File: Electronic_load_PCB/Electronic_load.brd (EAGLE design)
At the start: 121.9 x 88.6 mm, 111 parts, among them IC7 LM1117IMPX-5.0, J1 XT60-M, J2 B2B-XH, J3 B4B-XH, J4 B2B-XH, J5 B2B-XH, J6 B2B-XH, J7 B2B-XH, J8 B5B-XH, Q1 IRFP250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

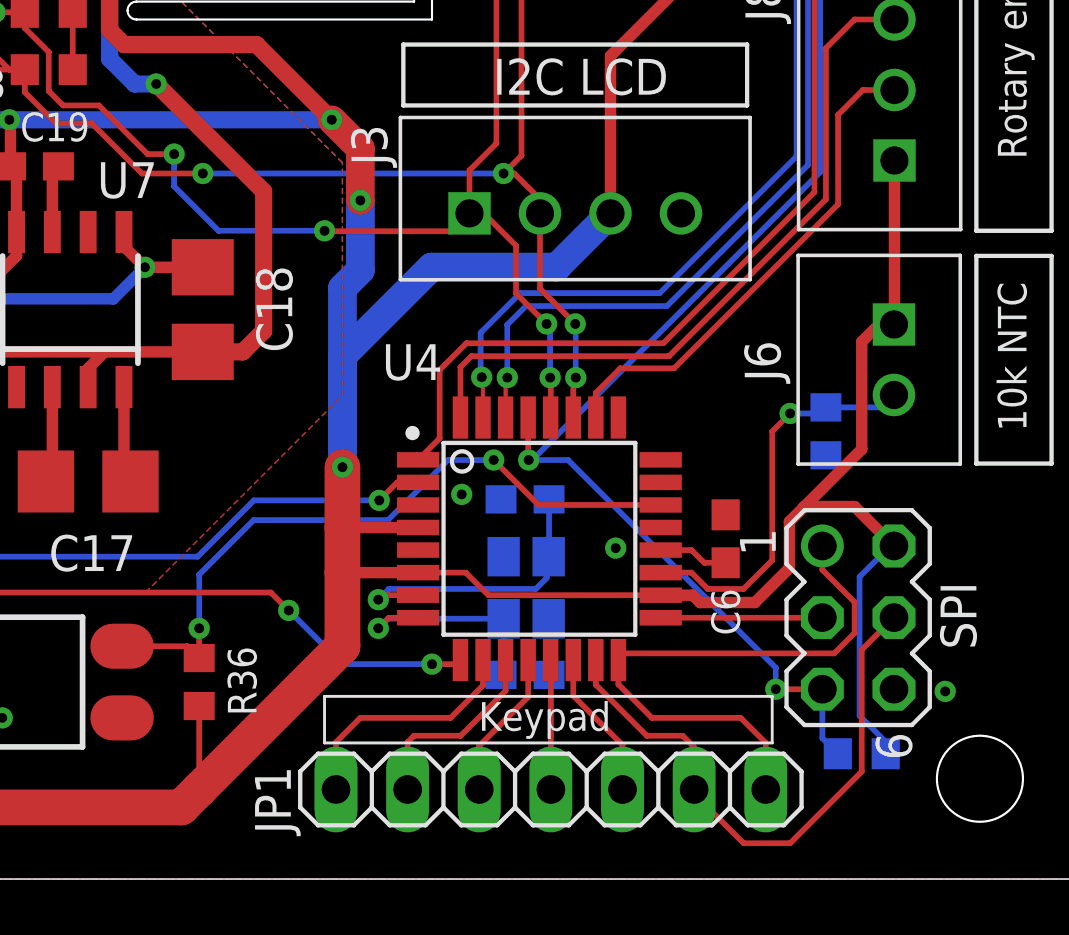
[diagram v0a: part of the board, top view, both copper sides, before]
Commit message: 9 pin keypad
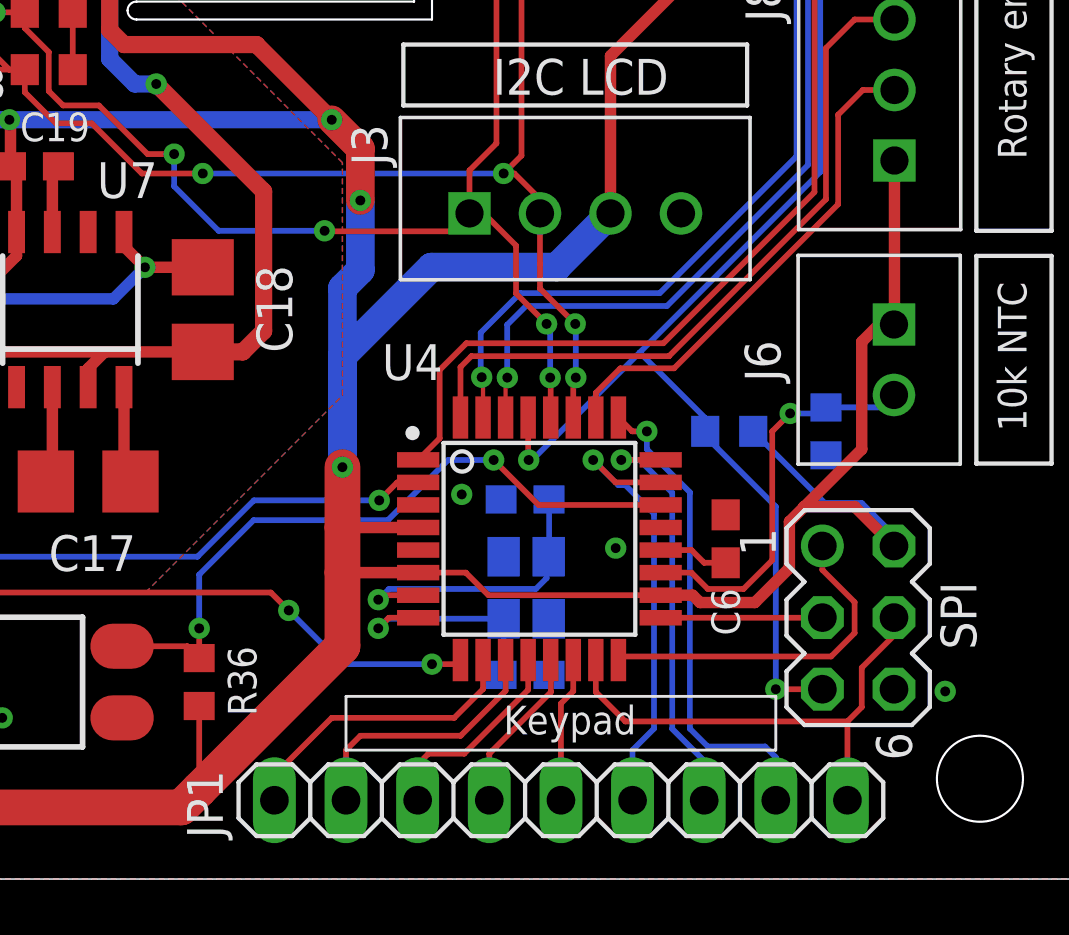
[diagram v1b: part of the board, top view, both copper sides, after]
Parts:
- JP1: device pinhead:1X07 -> pinhead:1X09
- moved R29 12.4 mm to (109.6, 15.9)
- moved JP1 0.52 mm to (103.6, 2.79)
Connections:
- removed net KP6/MOSI: JP1.6, SPI.4, U4.15
- removed net KP7/MISO: JP1.7, SPI.1, U4.16
- new net KP6: JP1.6, U4.23
- new net KP7: JP1.7, U4.24
- new net KP8: JP1.8, U4.25
- new net KP9/MOSI: JP1.9, SPI.4, U4.15
- new net MISO: SPI.1, U4.16
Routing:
- net KP7/MISO: track 20.9 -> 0.00 mm
- net KP6/MOSI: track 20.6 -> 0.00 mm
- net KP9/MOSI: track 0.00 -> 17.6 mm
- net KP8: track 0.00 -> 17.4 mm, vias 0 -> 1
- net KP6: track 0.00 -> 16.1 mm, vias 0 -> 1
- net KP7: track 0.00 -> 15.1 mm, vias 0 -> 1
- net MISO: track 0.00 -> 12.3 mm
- net KP2: track 7.00 -> 9.40 mm
- net KP3: track 5.31 -> 7.34 mm
- net KP1: track 8.62 -> 10.6 mm
- net 5V: track 278.3 -> 276.8 mm
- net KP4: track 4.59 -> 5.88 mm
- net RST: track 51.0 -> 50.0 mm

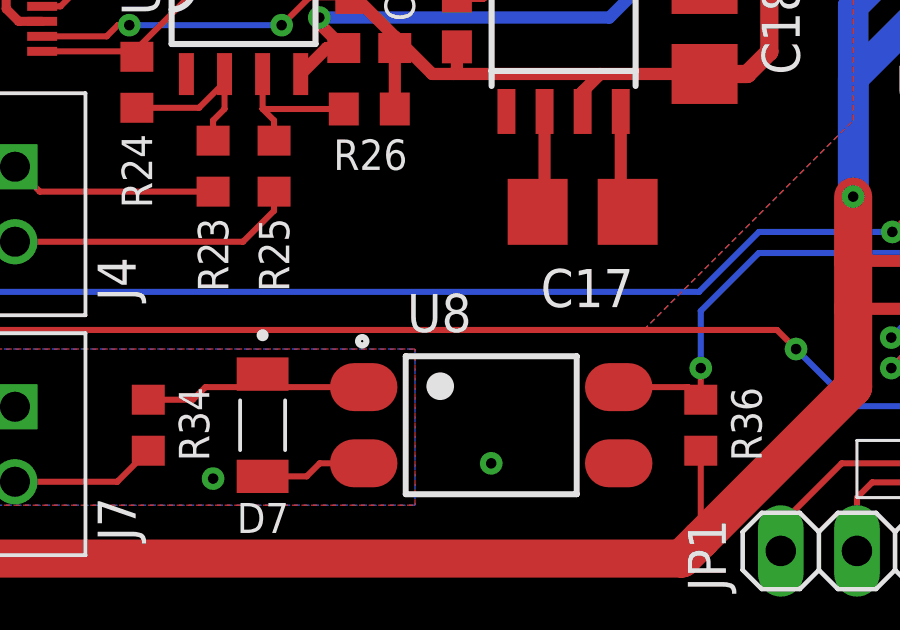
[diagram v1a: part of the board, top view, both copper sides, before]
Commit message: added missing component values
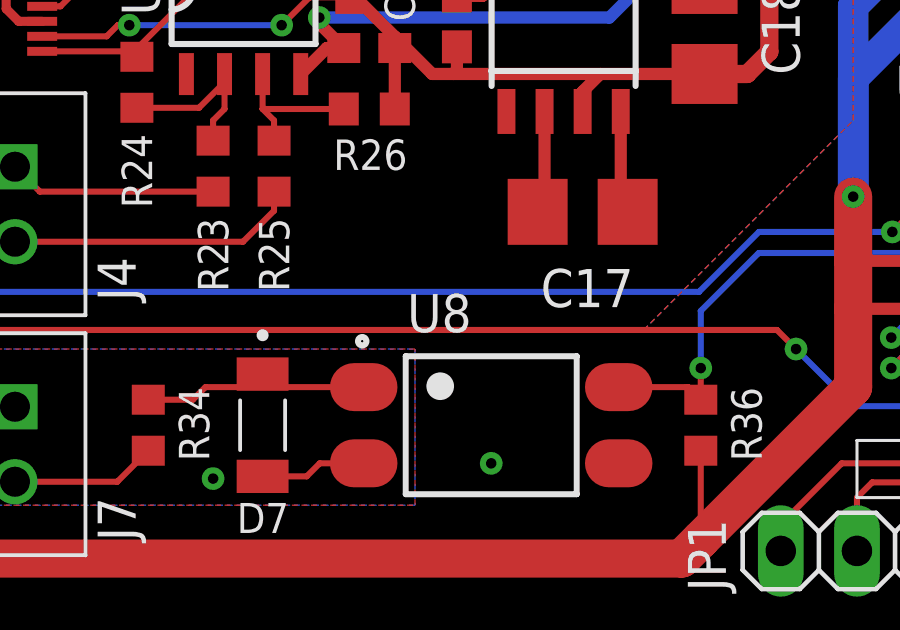
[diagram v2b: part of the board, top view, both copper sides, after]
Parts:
- R21: value (none) -> 15k
- R22, R41, R42, R43, R44: value (none) -> 1k
- R30: value (none) -> 470R
- R32: value 1k -> 68k
- R33: value 1k -> 18k
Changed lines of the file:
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@@
 <attribute name="VALUE" x="78.661" y="32.798" size="1.27" layer="27" rot="R180" align="bottom-right"/>
 </element>
-<element name="R21" library="rcl" library_urn="urn:adsk.eagle:library:334" package="R0603" package3d_urn="urn:adsk.eagle:package:23555/3" value="" x="77.851" y="35.814" smashed="yes">
+<element name="R21" library="rcl" library_urn="urn:adsk.eagle:library:334" package="R0603" package3d_urn="urn:adsk.eagle:package:23555/3" value="15k" x="77.851" y="35.814" smashed="yes">
 <attribute name="NAME" x="76.708" y="36.703" size="1.016" layer="25"/>
 <attribute name="POPULARITY" value="70" x="77.851" y="35.814" size="1.778" layer="27" display="off"/>
@@
 <attribute name="VALUE" x="77.216" y="33.909" size="1.27" layer="27"/>
 </element>
-<element name="R22" library="rcl" library_urn="urn:adsk.eagle:library:334" package="R0603" package3d_urn="urn:adsk.eagle:package:23555/3" value="" x="75.311" y="34.29" smashed="yes" rot="R90">
+<element name="R22" library="rcl" library_urn="urn:adsk.eagle:library:334" package="R0603" package3d_urn="urn:adsk.eagle:package:23555/3" value="1k" x="75.311" y="34.29" smashed="yes" rot="R90">
 <attribute name="NAME" x="75.819" y="30.099" size="1.016" layer="25" rot="R90"/>
 <attribute name="POPULARITY" value="70" x="75.311" y="34.29" size="1.778" layer="27" rot="R90" display="off"/>
@@
 <attribute name="VALUE" x="26.035" y="32.385" size="1.27" layer="28" rot="MR270"/>
 </element>
-<element name="R30" library="rcl" library_urn="urn:adsk.eagle:library:334" package="R0603" package3d_urn="urn:adsk.eagle:package:23555/3" value="" x="34.925" y="29.845" smashed="yes" rot="R90">
+<element name="R30" library="rcl" library_urn="urn:adsk.eagle:library:334" package="R0603" package3d_urn="urn:adsk.eagle:package:23555/3" value="470R" x="34.925" y="29.845" smashed="yes" rot="R90">
 <attribute name="NAME" x="36.83" y="28.575" size="1.016" layer="25" rot="R90"/>
 <attribute name="POPULARITY" value="70" x="34.925" y="29.845" size="1.778" layer="27" rot="R90" display="off"/>
@@
 <attribute name="VALUE" x="29.845" y="17.78" size="1.27" layer="28" rot="MR180"/>
 </element>
-<element name="R32" library="rcl" library_urn="urn:adsk.eagle:library:334" package="R0603" package3d_urn="urn:adsk.eagle:package:23555/3" value="1k" x="25.4" y="17.145" smashed="yes" rot="R90">
+<element name="R32" library="rcl" library_urn="urn:adsk.eagle:library:334" package="R0603" package3d_urn="urn:adsk.eagle:package:23555/3" value="68k" x="25.4" y="17.145" smashed="yes" rot="R90">
 <attribute name="NAME" x="24.13" y="15.875" size="1.016" layer="25" rot="R90"/>
 <attribute name="POPULARITY" value="70" x="25.4" y="17.145" size="1.778" layer="27" rot="R90" display="off"/>
@@
 <attribute name="VALUE" x="27.305" y="16.51" size="1.27" layer="27" rot="R90"/>
 </element>
-<element name="R33" library="rcl" library_urn="urn:adsk.eagle:library:334" package="R0603" package3d_urn="urn:adsk.eagle:package:23555/3" value="1k" x="25.4" y="20.32" smashed="yes" rot="R90">
+<element name="R33" library="rcl" library_urn="urn:adsk.eagle:library:334" package="R0603" package3d_urn="urn:adsk.eagle:package:23555/3" value="18k" x="25.4" y="20.32" smashed="yes" rot="R90">
 <attribute name="NAME" x="24.13" y="19.05" size="1.016" layer="25" rot="R90"/>
 <attribute name="POPULARITY" value="70" x="25.4" y="20.32" size="1.778" layer="27" rot="R90" display="off"/>
@@
 <attribute name="MF" value="Sharp Microelectronics" x="83.82" y="6.985" size="1.778" layer="27" display="off"/>
 <attribute name="MP" value="PC817X2NIP0F" x="83.82" y="6.985" size="1.778" layer="27" display="off"/>
+<attribute name="NAME" x="81.014759375" y="10.0908" size="1.27238125" layer="25"/>
 <attribute name="NAME" x="81.01816875" y="10.08701875" size="1.27083125" layer="25"/>
-<attribute name="NAME" x="81.014759375" y="10.0908" size="1.27238125" layer="25"/>
 <attribute name="PACKAGE" value="SMD-4 Sharp" x="83.82" y="6.985" size="1.778" layer="27" display="off"/>
 <attribute name="PRICE" value="None" x="83.82" y="6.985" size="1.778" layer="27" display="off"/>
@@
 <attribute name="VALUE" x="118.11" y="40.005" size="1.27" layer="27" rot="R90"/>
 </element>
-<element name="R41" library="rcl" library_urn="urn:adsk.eagle:library:334" package="R0603" package3d_urn="urn:adsk.eagle:package:23555/3" value="" x="62.738" y="22.86" smashed="yes" rot="R90">
+<element name="R41" library="rcl" library_urn="urn:adsk.eagle:library:334" package="R0603" package3d_urn="urn:adsk.eagle:package:23555/3" value="1k" x="62.738" y="22.86" smashed="yes" rot="R90">
 <attribute name="NAME" x="63.246" y="24.384" size="1.016" layer="25" rot="R90"/>
 <attribute name="POPULARITY" value="70" x="62.738" y="22.86" size="1.778" layer="27" rot="R90" display="off"/>
@@
 <attribute name="VALUE" x="64.643" y="22.225" size="1.27" layer="27" rot="R90"/>
 </element>
-<element name="R42" library="rcl" library_urn="urn:adsk.eagle:library:334" package="R0603" package3d_urn="urn:adsk.eagle:package:23555/3" value="" x="60.706" y="22.86" smashed="yes" rot="R90">
+<element name="R42" library="rcl" library_urn="urn:adsk.eagle:library:334" package="R0603" package3d_urn="urn:adsk.eagle:package:23555/3" value="1k" x="60.706" y="22.86" smashed="yes" rot="R90">
 <attribute name="NAME" x="61.214" y="24.384" size="1.016" layer="25" rot="R90"/>
 <attribute name="POPULARITY" value="70" x="60.706" y="22.86" size="1.778" layer="27" rot="R90" display="off"/>
@@
 <attribute name="VALUE" x="62.611" y="22.225" size="1.27" layer="27" rot="R90"/>
 </element>
-<element name="R43" library="rcl" library_urn="urn:adsk.eagle:library:334" package="R0603" package3d_urn="urn:adsk.eagle:package:23555/3" value="" x="58.674" y="22.86" smashed="yes" rot="R90">
+<element name="R43" library="rcl" library_urn="urn:adsk.eagle:library:334" package="R0603" package3d_urn="urn:adsk.eagle:package:23555/3" value="1k" x="58.674" y="22.86" smashed="yes" rot="R90">
 <attribute name="NAME" x="59.182" y="24.384" size="1.016" layer="25" rot="R90"/>
 <attribute name="POPULARITY" value="70" x="58.674" y="22.86" size="1.778" layer="27" rot="R90" display="off"/>
@@
 <attribute name="VALUE" x="60.579" y="22.225" size="1.27" layer="27" rot="R90"/>
 </element>
-<element name="R44" library="rcl" library_urn="urn:adsk.eagle:library:334" package="R0603" package3d_urn="urn:adsk.eagle:package:23555/3" value="" x="56.642" y="22.86" smashed="yes" rot="R90">
+<element name="R44" library="rcl" library_urn="urn:adsk.eagle:library:334" package="R0603" package3d_urn="urn:adsk.eagle:package:23555/3" value="1k" x="56.642" y="22.86" smashed="yes" rot="R90">
 <attribute name="NAME" x="57.15" y="24.384" size="1.016" layer="25" rot="R90"/>
 <attribute name="POPULARITY" value="70" x="56.642" y="22.86" size="1.778" layer="27" rot="R90" display="off"/>

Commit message: changed some resistor values
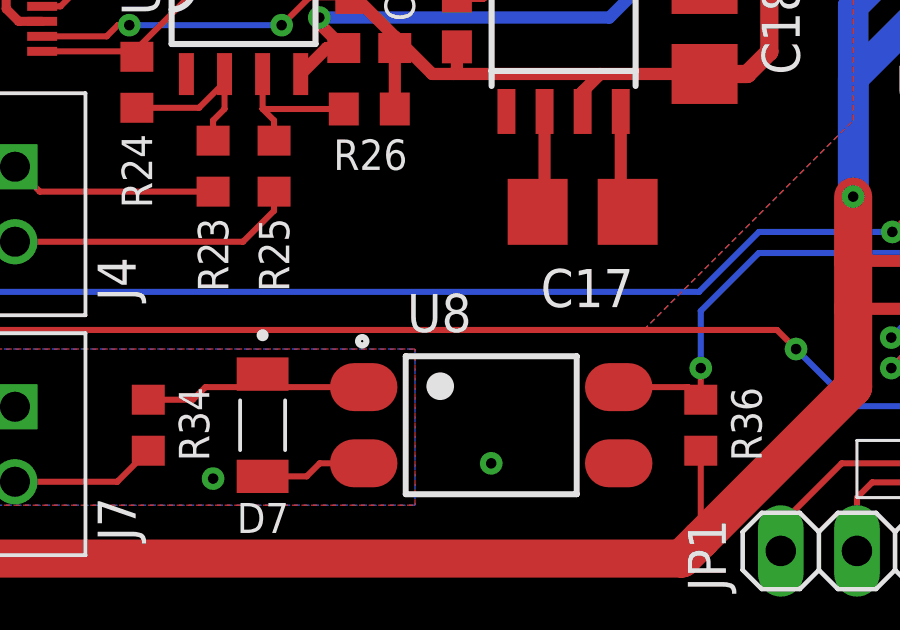
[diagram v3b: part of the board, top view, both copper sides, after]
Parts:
- R21: value 15k -> 10k
- R30: value 470R -> 1k
- R35: value 10k -> 47k
- R37, R38, R39, R40: value 1k -> 100k
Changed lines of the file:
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@@
 <attribute name="VALUE" x="78.661" y="32.798" size="1.27" layer="27" rot="R180" align="bottom-right"/>
 </element>
-<element name="R21" library="rcl" library_urn="urn:adsk.eagle:library:334" package="R0603" package3d_urn="urn:adsk.eagle:package:23555/3" value="15k" x="77.851" y="35.814" smashed="yes">
+<element name="R21" library="rcl" library_urn="urn:adsk.eagle:library:334" package="R0603" package3d_urn="urn:adsk.eagle:package:23555/3" value="10k" x="77.851" y="35.814" smashed="yes">
 <attribute name="NAME" x="76.708" y="36.703" size="1.016" layer="25"/>
 <attribute name="POPULARITY" value="70" x="77.851" y="35.814" size="1.778" layer="27" display="off"/>
@@
 <attribute name="VALUE" x="26.035" y="32.385" size="1.27" layer="28" rot="MR270"/>
 </element>
-<element name="R30" library="rcl" library_urn="urn:adsk.eagle:library:334" package="R0603" package3d_urn="urn:adsk.eagle:package:23555/3" value="470R" x="34.925" y="29.845" smashed="yes" rot="R90">
+<element name="R30" library="rcl" library_urn="urn:adsk.eagle:library:334" package="R0603" package3d_urn="urn:adsk.eagle:package:23555/3" value="1k" x="34.925" y="29.845" smashed="yes" rot="R90">
 <attribute name="NAME" x="36.83" y="28.575" size="1.016" layer="25" rot="R90"/>
 <attribute name="POPULARITY" value="70" x="34.925" y="29.845" size="1.778" layer="27" rot="R90" display="off"/>
@@
 <attribute name="VALUE" x="70.485" y="7.62" size="1.27" layer="27" rot="R270"/>
 </element>
-<element name="R35" library="rcl" library_urn="urn:adsk.eagle:library:334" package="R0603" package3d_urn="urn:adsk.eagle:package:23555/3" value="10k" x="113.03" y="15.875" smashed="yes" rot="MR90">
+<element name="R35" library="rcl" library_urn="urn:adsk.eagle:library:334" package="R0603" package3d_urn="urn:adsk.eagle:package:23555/3" value="47k" x="113.03" y="15.875" smashed="yes" rot="MR90">
 <attribute name="NAME" x="112.4966" y="17.4244" size="1.016" layer="26" rot="MR90"/>
 <attribute name="POPULARITY" value="70" x="113.03" y="15.875" size="1.778" layer="28" rot="MR90" display="off"/>
@@
 <attribute name="MF" value="Sharp Microelectronics" x="83.82" y="6.985" size="1.778" layer="27" display="off"/>
 <attribute name="MP" value="PC817X2NIP0F" x="83.82" y="6.985" size="1.778" layer="27" display="off"/>
+<attribute name="NAME" x="81.01816875" y="10.08701875" size="1.27083125" layer="25"/>
 <attribute name="NAME" x="81.014759375" y="10.0908" size="1.27238125" layer="25"/>
-<attribute name="NAME" x="81.01816875" y="10.08701875" size="1.27083125" layer="25"/>
 <attribute name="PACKAGE" value="SMD-4 Sharp" x="83.82" y="6.985" size="1.778" layer="27" display="off"/>
 <attribute name="PRICE" value="None" x="83.82" y="6.985" size="1.778" layer="27" display="off"/>
@@
 <attribute name="VALUE" x="57.785" y="36.449" size="1.27" layer="28" rot="MR270"/>
 </element>
-<element name="R37" library="rcl" library_urn="urn:adsk.eagle:library:334" package="R0603" package3d_urn="urn:adsk.eagle:package:23555/3" value="1k" x="58.42" y="34.925" smashed="yes" rot="MR0">
+<element name="R37" library="rcl" library_urn="urn:adsk.eagle:library:334" package="R0603" package3d_urn="urn:adsk.eagle:package:23555/3" value="100k" x="58.42" y="34.925" smashed="yes" rot="MR0">
 <attribute name="NAME" x="62.484" y="34.417" size="1.016" layer="26" rot="MR0"/>
 <attribute name="POPULARITY" value="70" x="58.42" y="34.925" size="1.016" layer="28" rot="MR0" display="off"/>
@@
 <attribute name="VALUE" x="57.785" y="32.385" size="1.27" layer="28" rot="MR270"/>
 </element>
-<element name="R38" library="rcl" library_urn="urn:adsk.eagle:library:334" package="R0603" package3d_urn="urn:adsk.eagle:package:23555/3" value="1k" x="58.42" y="36.957" smashed="yes" rot="MR0">
+<element name="R38" library="rcl" library_urn="urn:adsk.eagle:library:334" package="R0603" package3d_urn="urn:adsk.eagle:package:23555/3" value="100k" x="58.42" y="36.957" smashed="yes" rot="MR0">
 <attribute name="NAME" x="62.484" y="36.576" size="1.016" layer="26" rot="MR0"/>
 <attribute name="POPULARITY" value="70" x="66.04" y="44.577" size="1.016" layer="28" rot="MR0" display="off"/>
@@
 <attribute name="VALUE" x="65.405" y="27.051" size="1.27" layer="28" rot="MR90"/>
 </element>
-<element name="R39" library="rcl" library_urn="urn:adsk.eagle:library:334" package="R0603" package3d_urn="urn:adsk.eagle:package:23555/3" value="1k" x="67.818" y="32.004" smashed="yes" rot="MR180">
+<element name="R39" library="rcl" library_urn="urn:adsk.eagle:library:334" package="R0603" package3d_urn="urn:adsk.eagle:package:23555/3" value="100k" x="67.818" y="32.004" smashed="yes" rot="MR180">
 <attribute name="NAME" x="63.754" y="32.385" size="1.016" layer="26" rot="MR180"/>
 <attribute name="POPULARITY" value="70" x="60.198" y="24.384" size="1.016" layer="28" rot="MR180" display="off"/>
@@
 <attribute name="VALUE" x="64.643" y="35.179" size="1.27" layer="28" rot="MR90"/>
 </element>
-<element name="R40" library="rcl" library_urn="urn:adsk.eagle:library:334" package="R0603" package3d_urn="urn:adsk.eagle:package:23555/3" value="1k" x="67.818" y="34.036" smashed="yes" rot="MR180">
+<element name="R40" library="rcl" library_urn="urn:adsk.eagle:library:334" package="R0603" package3d_urn="urn:adsk.eagle:package:23555/3" value="100k" x="67.818" y="34.036" smashed="yes" rot="MR180">
 <attribute name="NAME" x="63.754" y="34.544" size="1.016" layer="26" rot="MR180"/>
 <attribute name="POPULARITY" value="70" x="60.198" y="26.416" size="1.016" layer="28" rot="MR180" display="off"/>
